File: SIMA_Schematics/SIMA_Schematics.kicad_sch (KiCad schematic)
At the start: 11 parts, among them U1 SIM800C, U2 Buck converter, U3 Buck converter

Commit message: Updaterade Arduino - SIM pins
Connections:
- net at U1.1 (UART1_TXD): now also A1.7 (D4); no longer A1.2 (D0/RX)
- net at R4.1: now also A1.8 (D5); no longer A1.1 (D1/TX)
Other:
- moved on the sheet: R4, R5
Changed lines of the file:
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@@
-	)
-	(junction
-		(at 111.76 76.2)
-		(diameter 0)
-		(color 0 0 0 0)
 	)
 	(junction
@@
 		(color 0 0 0 0)
 	)
+	(junction
+		(at 111.76 86.36)
+		(diameter 0)
+		(color 0 0 0 0)
+	)
 	(wire
 		(pts
@@
 	(wire
 		(pts
-			(xy 119.38 64.77) (xy 121.92 64.77)
-		)
-		(stroke
-			(width 0)
-			(type default)
-		)
-	)
-	(wire
-		(pts
 			(xy 212.09 21.59) (xy 212.09 114.3)
 		)
@@
 	(wire
 		(pts
-			(xy 101.6 76.2) (xy 111.76 76.2)
+			(xy 119.38 73.66) (xy 119.38 76.2)
 		)
 		(stroke
@@
 	(wire
 		(pts
-			(xy 109.22 73.66) (xy 109.22 66.04)
-		)
-		(stroke
-			(width 0)
-			(type default)
-		)
-	)
-	(wire
-		(pts
 			(xy 76.2 46.99) (xy 76.2 55.88)
 		)
@@
 	(wire
 		(pts
+			(xy 107.95 86.36) (xy 111.76 86.36)
+		)
+		(stroke
+			(width 0)
+			(type default)
+		)
+	)
+	(wire
+		(pts
 			(xy 135.89 118.11) (xy 135.89 114.3)
 		)
@@
 	(wire
 		(pts
-			(xy 121.92 68.58) (xy 123.19 68.58)
+			(xy 119.38 76.2) (xy 123.19 76.2)
 		)
 		(stroke
@@
 	(wire
 		(pts
-			(xy 121.92 67.31) (xy 121.92 68.58)
-		)
-		(stroke
-			(width 0)
-			(type default)
-		)
-	)
-	(wire
-		(pts
 			(xy 168.91 81.28) (xy 180.34 81.28)
 		)
@@
 	(wire
 		(pts
-			(xy 119.38 66.04) (xy 119.38 64.77)
-		)
-		(stroke
-			(width 0)
-			(type default)
-		)
-	)
-	(wire
-		(pts
 			(xy 140.97 43.18) (xy 142.24 43.18)
 		)
@@
 	(wire
 		(pts
-			(xy 109.22 66.04) (xy 119.38 66.04)
-		)
-		(stroke
-			(width 0)
-			(type default)
-		)
-	)
-	(wire
-		(pts
-			(xy 119.38 68.58) (xy 119.38 67.31)
-		)
-		(stroke
-			(width 0)
-			(type default)
-		)
-	)
-	(wire
-		(pts
 			(xy 153.67 53.34) (xy 154.94 53.34)
 		)
@@
 	(wire
 		(pts
-			(xy 111.76 83.82) (xy 111.76 118.11)
+			(xy 111.76 93.98) (xy 111.76 118.11)
 		)
 		(stroke
@@
 	(wire
 		(pts
+			(xy 111.76 78.74) (xy 123.19 78.74)
+		)
+		(stroke
+			(width 0)
+			(type default)
+		)
+	)
+	(wire
+		(pts
 			(xy 142.24 43.18) (xy 142.24 40.64)
 		)
@@
 	(wire
 		(pts
+			(xy 107.95 76.2) (xy 101.6 76.2)
+		)
+		(stroke
+			(width 0)
+			(type default)
+		)
+	)
+	(wire
+		(pts
 			(xy 153.67 82.55) (xy 153.67 88.9)
 		)
@@
 	(wire
 		(pts
+			(xy 107.95 76.2) (xy 107.95 86.36)
+		)
+		(stroke
+			(width 0)
+			(type default)
+		)
+	)
+	(wire
+		(pts
 			(xy 76.2 46.99) (xy 152.4 46.99)
 		)
@@
 	(wire
 		(pts
-			(xy 121.92 64.77) (xy 121.92 66.04)
-		)
-		(stroke
-			(width 0)
-			(type default)
-		)
-	)
-	(wire
-		(pts
-			(xy 101.6 73.66) (xy 109.22 73.66)
+			(xy 101.6 73.66) (xy 119.38 73.66)
 		)
 		(stroke
@@
 	(wire
 		(pts
-			(xy 119.38 67.31) (xy 121.92 67.31)
-		)
-		(stroke
-			(width 0)
-			(type default)
-		)
-	)
-	(wire
-		(pts
 			(xy 168.91 81.28) (xy 168.91 91.44)
 		)
@@
 		(pts
 			(xy 180.34 76.2) (xy 166.37 76.2)
-		)
-		(stroke
-			(width 0)
-			(type default)
-		)
-	)
-	(wire
-		(pts
-			(xy 111.76 68.58) (xy 119.38 68.58)
-		)
-		(stroke
-			(width 0)
-			(type default)
-		)
-	)
-	(wire
-		(pts
-			(xy 121.92 66.04) (xy 123.19 66.04)
 		)
 		(stroke
@@
 	(symbol
 		(lib_id "Device:R")
-		(at 111.76 72.39 0)
+		(at 111.76 82.55 0)
 		(unit 1)
 		(exclude_from_sim no)
@@
 		(fields_autoplaced yes)
 		(property "Reference" "R4"
-			(at 114.3 71.1199 0)
+			(at 114.3 81.2799 0)
 			(effects
 				(font
@@
 		)
 		(property "Value" "2 kohm"
-			(at 114.3 73.6599 0)
+			(at 114.3 83.8199 0)
 			(effects
 				(font
@@
 		)
 		(property "Footprint" ""
-			(at 109.982 72.39 90)
+			(at 109.982 82.55 90)
 			(effects
 				(font
@@
 		)
 		(property "Datasheet" "~"
-			(at 111.76 72.39 0)
+			(at 111.76 82.55 0)
 			(effects
 				(font
@@
 		)
 		(property "Description" "Resistor"
-			(at 111.76 72.39 0)
+			(at 111.76 82.55 0)
 			(effects
 				(font
@@
 	(symbol
 		(lib_id "Device:R")
-		(at 111.76 80.01 0)
+		(at 111.76 90.17 0)
 		(unit 1)
 		(exclude_from_sim no)
@@
 		(fields_autoplaced yes)
 		(property "Reference" "R5"
-			(at 114.3 78.7399 0)
+			(at 114.3 88.8999 0)
 			(effects
 				(font
@@
 		)
 		(property "Value" "1 kohm"
-			(at 114.3 81.2799 0)
+			(at 114.3 91.4399 0)
 			(effects
 				(font
@@
 		)
 		(property "Footprint" ""
-			(at 109.982 80.01 90)
+			(at 109.982 90.17 90)
 			(effects
 				(font
@@
 		)
 		(property "Datasheet" "~"
-			(at 111.76 80.01 0)
+			(at 111.76 90.17 0)
 			(effects
 				(font
@@
 		)
 		(property "Description" "Resistor"
-			(at 111.76 80.01 0)
-			(effects
-				(font
+			(at 111.76 90.17 0)
+			(effects
+				(font

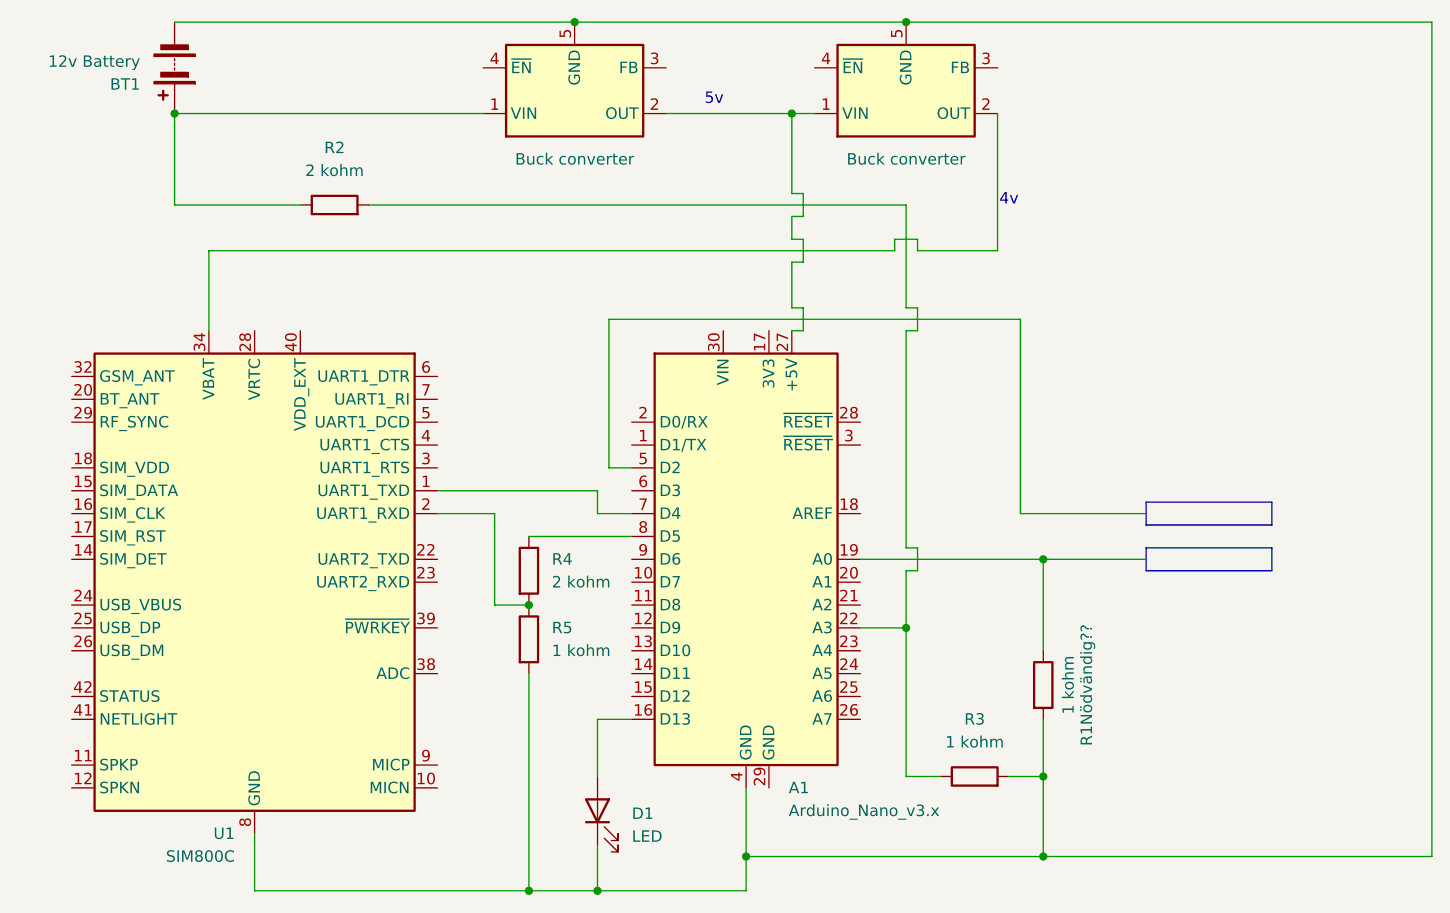
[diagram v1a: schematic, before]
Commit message: Uppdaterade schematics
Uppdaterade waterDetect pin till 5v eller D3?
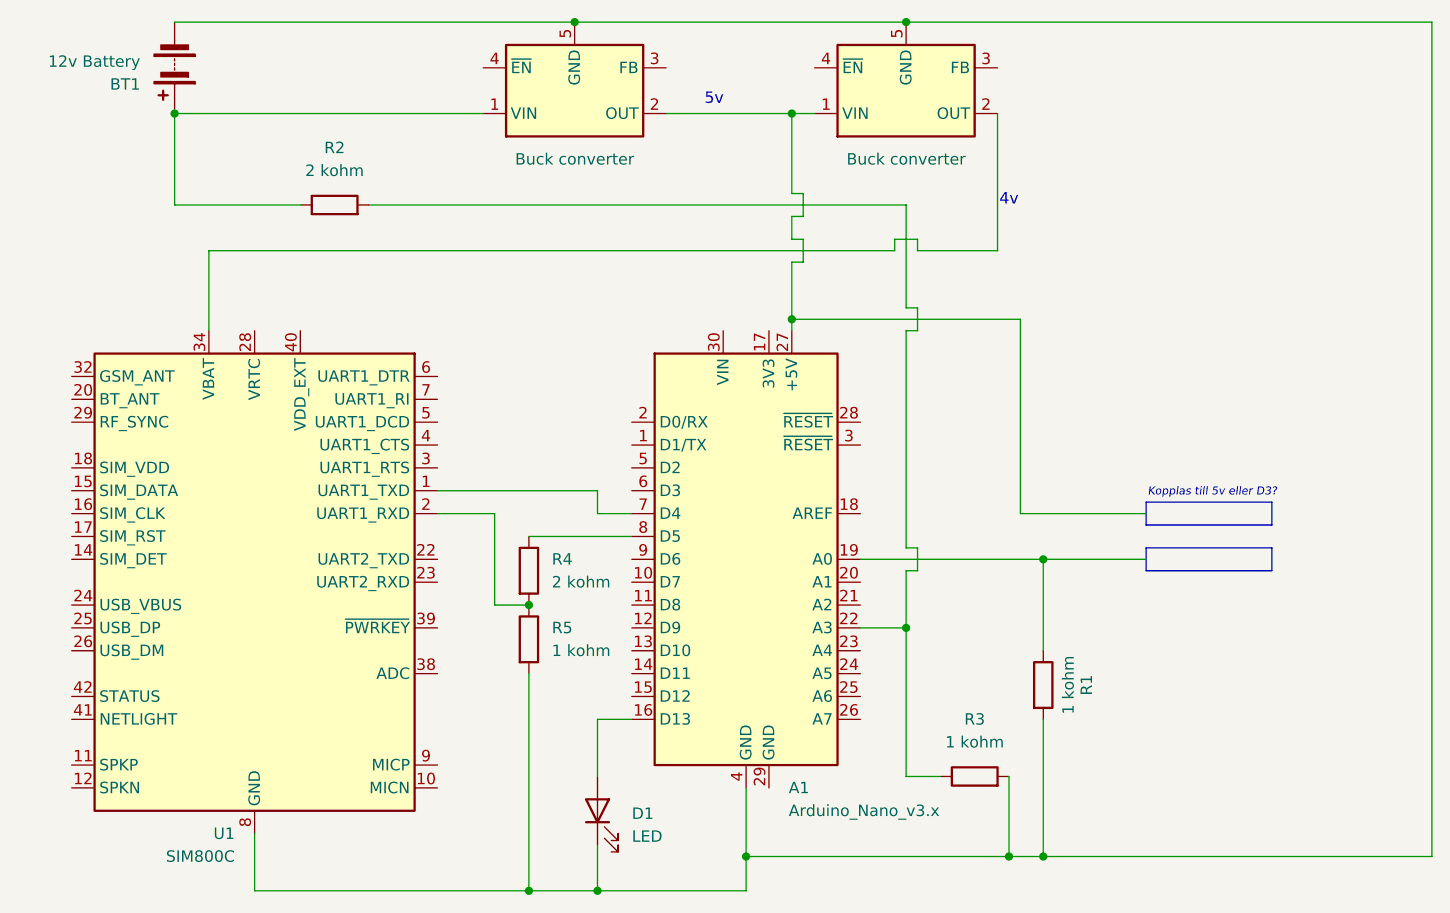
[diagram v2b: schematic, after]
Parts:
- gave numbers to parts that had none: 1
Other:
- note added: "Kopplas till 5v eller D3?"
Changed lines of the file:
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@@
+	)
+	(junction
+		(at 140.97 54.61)
+		(diameter 0)
+		(color 0 0 0 0)
 	)
 	(junction
@@
 	)
 	(junction
-		(at 168.91 105.41)
+		(at 165.1 114.3)
 		(diameter 0)
 		(color 0 0 0 0)
@@
 	(wire
 		(pts
-			(xy 168.91 105.41) (xy 168.91 114.3)
+			(xy 168.91 99.06) (xy 168.91 114.3)
 		)
 		(stroke
@@
 	(wire
 		(pts
+			(xy 165.1 105.41) (xy 165.1 114.3)
+		)
+		(stroke
+			(width 0)
+			(type default)
+		)
+	)
+	(wire
+		(pts
 			(xy 153.67 21.59) (xy 212.09 21.59)
 		)
@@
 	(wire
 		(pts
-			(xy 165.1 105.41) (xy 168.91 105.41)
-		)
-		(stroke
-			(width 0)
-			(type default)
-		)
-	)
-	(wire
-		(pts
 			(xy 107.95 86.36) (xy 111.76 86.36)
 		)
@@
 	(wire
 		(pts
-			(xy 140.97 53.34) (xy 140.97 48.26)
+			(xy 140.97 48.26) (xy 140.97 54.61)
 		)
 		(stroke
@@
 	(wire
 		(pts
+			(xy 140.97 54.61) (xy 166.37 54.61)
+		)
+		(stroke
+			(width 0)
+			(type default)
+		)
+	)
+	(wire
+		(pts
 			(xy 212.09 114.3) (xy 168.91 114.3)
 		)
@@
 	(wire
 		(pts
+			(xy 165.1 114.3) (xy 135.89 114.3)
+		)
+		(stroke
+			(width 0)
+			(type default)
+		)
+	)
+	(wire
+		(pts
 			(xy 116.84 21.59) (xy 153.67 21.59)
 		)
@@
 	(wire
 		(pts
-			(xy 142.24 53.34) (xy 140.97 53.34)
-		)
-		(stroke
-			(width 0)
-			(type default)
-		)
-	)
-	(wire
-		(pts
 			(xy 153.67 105.41) (xy 157.48 105.41)
 		)
@@
 	(wire
 		(pts
-			(xy 142.24 55.88) (xy 142.24 53.34)
+			(xy 140.97 55.88) (xy 140.97 54.61)
 		)
 		(stroke
@@
 	(wire
 		(pts
-			(xy 120.65 71.12) (xy 123.19 71.12)
-		)
-		(stroke
-			(width 0)
-			(type default)
-		)
-	)
-	(wire
-		(pts
 			(xy 153.67 41.91) (xy 153.67 53.34)
 		)
@@
 	(wire
 		(pts
-			(xy 168.91 114.3) (xy 135.89 114.3)
+			(xy 168.91 114.3) (xy 165.1 114.3)
 		)
 		(stroke
@@
 	(wire
 		(pts
-			(xy 120.65 54.61) (xy 120.65 71.12)
-		)
-		(stroke
-			(width 0)
-			(type default)
-		)
-	)
-	(wire
-		(pts
 			(xy 101.6 73.66) (xy 119.38 73.66)
 		)
@@
 	(wire
 		(pts
-			(xy 120.65 54.61) (xy 166.37 54.61)
-		)
-		(stroke
-			(width 0)
-			(type default)
-		)
-	)
-	(wire
-		(pts
 			(xy 123.19 99.06) (xy 119.38 99.06)
 		)
@@
 	(wire
 		(pts
-			(xy 140.97 55.88) (xy 142.24 55.88)
-		)
-		(stroke
-			(width 0)
-			(type default)
-		)
-	)
-	(wire
-		(pts
 			(xy 168.91 81.28) (xy 168.91 91.44)
 		)
@@
 		(pts
 			(xy 72.39 41.91) (xy 86.36 41.91)
-		)
-		(stroke
-			(width 0)
-			(type default)
-		)
-	)
-	(wire
-		(pts
-			(xy 168.91 99.06) (xy 168.91 105.41)
 		)
 		(stroke
@@
 			(font
 				(size 1.27 1.27)
+			)
+		)
+	)
+	(text "Kopplas till 5v eller D3?"
+		(exclude_from_sim no)
+		(at 187.706 73.914 0)
+		(effects
+			(font
+				(size 0.889 0.889)
+				(italic yes)
+				(color 0 0 0 1)
 			)
 		)
@@
 		(on_board yes)
 		(dnp no)
-		(property "Reference" "R1Nödvändig??"
+		(property "Reference" "R1"
 			(at 173.736 95.25 90)
 			(effects
@@
 			(project ""
 				(path "/be6829d7-daf3-4649-8621-8128d8bc6168"
-					(reference "R1Nödvändig??")
+					(reference "R1")
 					(unit 1)
 				)

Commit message: uppdtaerad spänningsdelare
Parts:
- R4: value 2 kohm -> 560 ohm
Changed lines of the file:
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@@
 			)
 		)
-		(property "Value" "2 kohm"
+		(property "Value" "560 ohm"
 			(at 114.3 83.8199 0)
 			(effects

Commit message: Uppdaterade namn sim modul i cad
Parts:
- U1: value SIM800C -> SIM7670E
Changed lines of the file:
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@@
 			)
 		)
-		(property "Value" "SIM800C"
+		(property "Value" "SIM7670E"
 			(at 79.0859 114.3 0)
 			(effects
